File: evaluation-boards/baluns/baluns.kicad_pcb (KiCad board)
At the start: 4 copper layers, 23 x 100 mm, 178 parts, among them J1 CONN_COAXIAL, J10 CONN_COAXIAL, J11 CONN_COAXIAL, J12 CONN_COAXIAL, J13 CONN_COAXIAL, J14 CONN_COAXIAL, J15 CONN_COAXIAL, J16 CONN_COAXIAL, J17 CONN_COAXIAL, J18 CONN_COAXIAL, J2 CONN_COAXIAL, J3 CONN_COAXIAL, J4 CONN_COAXIAL, J5 CONN_COAXIAL, J6 CONN_COAXIAL, J7 CONN_COAXIAL, J8 CONN_COAXIAL, J9 CONN_COAXIAL, P1 Conn_01x02, P2 Conn_01x02, P3 Conn_01x02, P4 Conn_01x02, P5 Conn_01x02, Q1 BFR840, Q2 BFR840, Q3 BFR840, Q4 BFR840, Q5 BFP840ESD, Q6 BFP840ESD, Q7 BFP840ESD, Q8 BFP840ESD, T1 B0310J50100AHF, T2 B0310J50100AHF

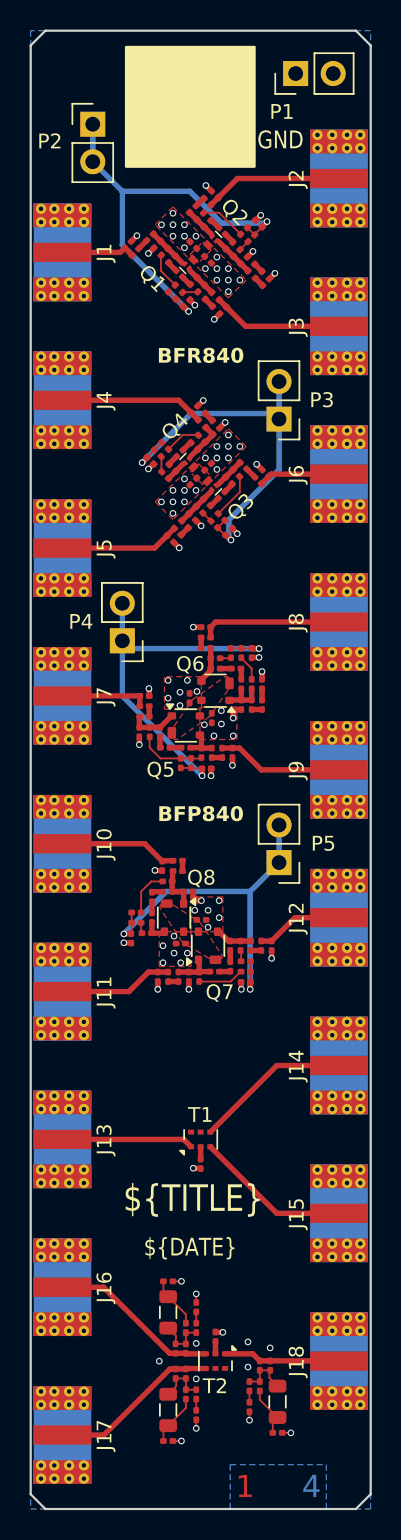
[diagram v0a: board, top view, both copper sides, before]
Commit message: Update baluns board
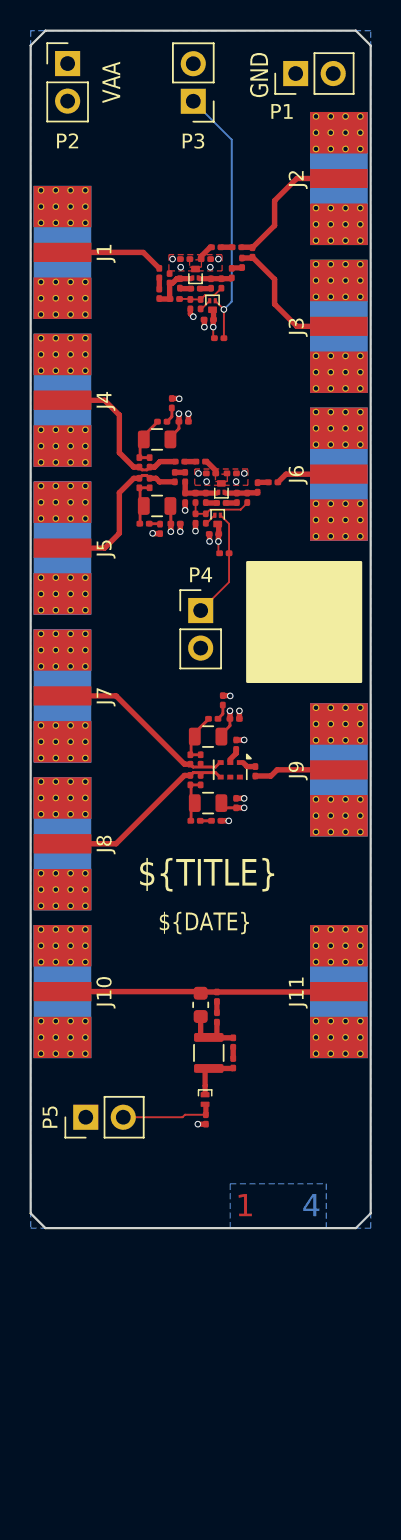
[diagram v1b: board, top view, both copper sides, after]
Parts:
- removed C10, C11, C12, C13, C17, C19, C20, C21, C22, C23, C24, C26, C27, C29, C31, C32, C35, C36, C37, C38, C39, C40, C44, C45, C47, C48, C7, C8, C9: 1 uF, Capacitor_SMD:C_0201_0603Metric
- removed C14, C15, C16, C18, C30, C33, C34, C43: 0.3 pF, Capacitor_SMD:C_0201_0603Metric
- removed J12, J13, J14, J15, J16, J17, J18: CONN_COAXIAL, sma-variants:SMA-EDGE-1.3mm-pad-1.05mm-gap-2.6mm-keepout
- removed L10: 18 nH, Inductor_SMD:L_0201_0603Metric
- removed L11: L, Inductor_SMD:L_0805_2012Metric
- removed L12, L9: L, Inductor_SMD:L_0201_0603Metric
- removed L14: 5.6 nH, Inductor_SMD:L_0201_0603Metric
- removed Q1, Q2, Q3, Q4: BFR840, eval:TSLP-3-9
- removed Q5, Q6, Q7, Q8: BFP840ESD, eval:SOT-343-4-3
- removed R10, R24, R46, R59, R71, R77, R79, R8, R80, R83: 220, Resistor_SMD:R_0201_0603Metric
- removed R11, R13, R19, R20, R26, R27, R30, R31, R32, R33, R36, R42, R47, R48, R49, R50, R51, R52, R55, R56, R60, R61, R62, R69, R72, R78, R81, R84, R85, R86: 0, Resistor_SMD:R_0201_0603Metric
- removed R14, R21, R37, R43, R6, R63, R73: 4.3k, Resistor_SMD:R_0201_0603Metric
- removed R15, R22, R38, R44, R64, R74, R9: 2.4k, Resistor_SMD:R_0201_0603Metric
- removed R16, R39, R66: 300, Resistor_SMD:R_0201_0603Metric
- removed R17, R40, R70: 200, Resistor_SMD:R_0201_0603Metric
- removed R18, R75, R82: 6.8k, Resistor_SMD:R_0201_0603Metric
- removed R23, R45, R7, R76: 470, Resistor_SMD:R_0201_0603Metric
- removed R25, R53: 43, Resistor_SMD:R_0201_0603Metric
- removed R28, R41, R54, R58, R67, R68: 82, Resistor_SMD:R_0201_0603Metric
- removed T1: B0310J50100AHF, RF_Converter:Anaren_0805_2012Metric-6
- added C112: 8p2, Capacitor_SMD:C_0201_0603Metric, F.Cu at (143.7, 133.4)
- added C171: 1 uF, Capacitor_SMD:C_0201_0603Metric, F.Cu at (141.8, 138.7)
- added C202: 2.2nF, Capacitor_SMD:C_0201_0603Metric, F.Cu at (138.9, 91.5)
- added C203: 8p2, Capacitor_SMD:C_0201_0603Metric, F.Cu at (137.7, 98.3)
- added C207: 1 uF, Capacitor_SMD:C_0201_0603Metric, F.Cu at (142.9, 97.0)
- added C208: 1 uF, Capacitor_SMD:C_0201_0603Metric, F.Cu at (144.3, 80.7)
- added C210: 1 uF, Capacitor_SMD:C_0201_0603Metric, F.Cu at (139.8, 95.2)
- added C211: 1 uF, Capacitor_SMD:C_0201_0603Metric, F.Cu at (141.2, 98.0)
- added C212: 1 uF, Capacitor_SMD:C_0201_0603Metric, F.Cu at (140.8, 83.5)
- added C213: 1 uF, Capacitor_SMD:C_0201_0603Metric, F.Cu at (143.9, 79.7)
- added C214: 1 uF, Capacitor_SMD:C_0201_0603Metric, F.Cu at (142.1, 84.5)
- added C215: 1 uF, Capacitor_SMD:C_0201_0603Metric, F.Cu at (142.4, 99.0)
- added D10: Schottky, eval:TSLP-2-19, F.Cu at (141.8, 137.3)
- added L19: 47uH, eval:L_Taiyo-Yuden_A251818, F.Cu at (142.1, 134.2)
- added L20: 33 nH, Inductor_SMD:L_0201_0603Metric, F.Cu at (142.6, 130.3)
- added L29: 100uH, eval:L_TDK_MLZ2012_h1.25mm, F.Cu at (138.6, 97.2)
- added L30: 56 nH, Inductor_SMD:L_0201_0603Metric, F.Cu at (138.1, 95.6)
- added Q15: BFR840, eval:TSLP-3-9, F.Cu at (141.2, 81.5)
- added Q16: Q_PMOS_GSD, eval:TSLP-3-9, F.Cu at (142.3, 83.5)
- added Q17: BFR840, eval:TSLP-3-9, F.Cu at (142.9, 96.0)
- added Q18: Q_PMOS_GSD, eval:TSLP-3-9, F.Cu at (142.7, 98.0)
- added R142: 0, Resistor_SMD:R_0201_0603Metric, F.Cu at (137.3, 95.6)
- added R143: 0, Resistor_SMD:R_0201_0603Metric, F.Cu at (138.8, 98.7)
- added R144: 0, Resistor_SMD:R_0201_0603Metric, F.Cu at (137.3, 94.2)
- added R147: 100, Resistor_SMD:R_0201_0603Metric, F.Cu at (139.6, 90.2)
- added R152: 330, Resistor_SMD:R_0201_0603Metric, F.Cu at (139.4, 81.8)
- added R153: 120, Resistor_SMD:R_0201_0603Metric, F.Cu at (140.1, 82.1)
- added R154: 33k, Resistor_SMD:R_0201_0603Metric, F.Cu at (142.8, 85.8)
- added R155: 100, Resistor_SMD:R_0201_0603Metric, F.Cu at (142.2, 82.1)
- added R156: 220, Resistor_SMD:R_0201_0603Metric, F.Cu at (142.9, 82.1)
- added R157: 750, Resistor_SMD:R_0201_0603Metric, F.Cu at (139.8, 83.2)
- added R158: 100, Resistor_SMD:R_0201_0603Metric, F.Cu at (141.8, 80.5)
- added R159: 100, Resistor_SMD:R_0201_0603Metric, F.Cu at (140.4, 80.5)
- added R160: 51, Resistor_SMD:R_0201_0603Metric, F.Cu at (143.6, 81.4)
- added R161: 10, Resistor_SMD:R_0201_0603Metric, F.Cu at (142.6, 79.7)
- added R162: 0, Resistor_SMD:R_0201_0603Metric, F.Cu at (138.7, 82.8)
- added R163: 0, Resistor_SMD:R_0201_0603Metric, F.Cu at (141.5, 83.5)
- added R164: 3.3k, Resistor_SMD:R_0201_0603Metric, F.Cu at (140.4, 96.6)
- added R165: 120, Resistor_SMD:R_0201_0603Metric, F.Cu at (141.8, 96.6)
- added R166: 100, Resistor_SMD:R_0201_0603Metric, F.Cu at (142.2, 95.0)
- added R167: 4k7, Resistor_SMD:R_0201_0603Metric, F.Cu at (141.2, 96.6)
- added R168: 100, Resistor_SMD:R_0201_0603Metric, F.Cu at (143.6, 95.0)
- added R169: 10, Resistor_SMD:R_0201_0603Metric, F.Cu at (141.5, 94.2)
- added R170: 10, Resistor_SMD:R_0201_0603Metric, F.Cu at (140.4, 95.2)
- added R171: 0, Resistor_SMD:R_0201_0603Metric, F.Cu at (141.8, 98.0)
- added R172: 0, Resistor_SMD:R_0201_0603Metric, F.Cu at (145.3, 95.9)
- added R173: 220, Resistor_SMD:R_0201_0603Metric, F.Cu at (144.7, 96.6)
- C1, C2, C5, C6: value 0.3 pF -> 1 uF
- C3: value 0.3 pF -> 8p2
- C4: value 0.3 pF -> 2.2nF
- J1, J10, J11, J2, J3, J4, J5, J6, J7, J8, J9: footprint sma-variants:SMA-EDGE-1.3mm-pad-1.05mm-gap-2.6mm-keepout -> eval:SMA_MyAntenna_A-SMA-KE-16.5A_EdgeMount
- L1: value 18 nH -> DNP
- L13: value L -> 62nH; footprint Inductor_SMD:L_0805_2012Metric -> Inductor_SMD:L_0603_1608Metric
- L2: value 5.6 nH -> 100uH; footprint Inductor_SMD:L_0201_0603Metric -> eval:L_TDK_MLZ2012_h1.25mm
- L3: value 18 nH -> 56 nH
- L4: value 5.6 nH -> 2.4 nH
- L5: value 18 nH -> 100uH; footprint Inductor_SMD:L_0201_0603Metric -> eval:L_TDK_MLZ2012_h1.25mm
- L6: value 5.6 nH -> 56 nH
- L7: value L -> 100uH; footprint Inductor_SMD:L_0201_0603Metric -> eval:L_TDK_MLZ2012_h1.25mm
- L8: value L -> 56 nH; footprint Inductor_SMD:L_0805_2012Metric -> Inductor_SMD:L_0201_0603Metric
- R1: value 82 -> 33k
- R12: value 0 -> 220
- R2: value 2.4k -> 0
- R3: value 4.3k -> 51
- R35: value 82 -> 220
- R4: value 300 -> 100
- R5: value 200 -> 10
- T2: value B0310J50100AHF -> RF_BALUN
- moved C49 62.7 mm to (140.1, 94.2), turned to 180 degrees
- moved R35 54.4 mm to (143.7, 134.8), turned to 90 degrees
- moved C42 50.2 mm to (140.3, 91.5), turned to 0 degrees
- moved L8 44.1 mm to (141.5, 114.3)
- moved L7 43.2 mm to (142.0, 112.8), turned to 180 degrees
- moved T2 40.0 mm to (143.5, 115.0)
- moved C3 39.2 mm to (141.2, 118.5), turned to 0 degrees
- moved R2 38.0 mm to (142.6, 118.5), turned to 180 degrees
- moved R5 36.7 mm to (140.8, 114.3), turned to -90 degrees
- moved R3 35.8 mm to (140.8, 115.7), turned to 90 degrees
- moved C2 35.5 mm to (143.8, 111.5), turned to 0 degrees
- moved C1 33.3 mm to (143.9, 117.2), turned to 90 degrees
- moved R4 31.7 mm to (143.0, 110.3), turned to 90 degrees
- moved C4 29.7 mm to (142.3, 111.5), turned to 180 degrees
- moved C41 29.1 mm to (139.8, 98.3), turned to 0 degrees
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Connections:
- C1 pad 1: Net-(J3-In) -> VAA
- C2 pad 1: Net-(J2-In) -> VAA
- C28 pad 1: Net-(J6-In) -> Net-(C28-Pad1)
- C28 pad 2: Net-(C28-Pad2) -> Net-(J1-In)
- C3 pad 1: Net-(J1-In) -> Net-(C3-Pad1)
- C3 pad 2: GND -> Net-(C3-Pad2)
- C4 pad 1: Net-(C21-Pad2) -> Net-(C4-Pad1)
- C4 pad 2: GND -> Net-(C4-Pad2)
- C41 pad 1: Net-(J12-In) -> VAA
- C41 pad 2: Net-(C41-Pad2) -> GND
- C42 pad 1: GND -> VAA
- C42 pad 2: Net-(T1-GND) -> GND
- C46 pad 2: Net-(Q1-B) -> Net-(J6-In)
- C49 pad 2: Net-(C49-Pad2) -> Net-(J4-In)
- C5 pad 1: Net-(J7-In) -> GND
- C5 pad 2: GND -> Net-(T2-GND)
- C6 pad 1: Net-(C6-Pad1) -> Net-(J9-In)
- C6 pad 2: GND -> Net-(C6-Pad2)
- J11 pad 1: Net-(J11-In) -> Net-(J10-In)
- L1 pad 1: Net-(C9-Pad1) -> Net-(J2-In)
- L1 pad 2: Net-(L1-Pad2) -> Net-(J3-In)
- L13 pad 1: Net-(C49-Pad1) -> Net-(C112-Pad2)
- L13 pad 2: Net-(L13-Pad2) -> Net-(J10-In)
- L2 pad 1: Net-(C11-Pad1) -> VAA
- L2 pad 2: Net-(L2-Pad2) -> Net-(C202-Pad2)
- L3 pad 1: Net-(L3-Pad1) -> Net-(C202-Pad2)
- L3 pad 2: Net-(Q4-C) -> Net-(J4-In)
- L5 pad 1: Net-(C37-Pad1) -> VAA
- L5 pad 2: Net-(L5-Pad2) -> Net-(C3-Pad1)
- L6 pad 1: Net-(C39-Pad1) -> Net-(C3-Pad1)
- L6 pad 2: Net-(L6-Pad2) -> Net-(J8-In)
- L7 pad 1: Net-(J17-In) -> VAA
- L7 pad 2: Net-(C47-Pad1) -> Net-(C4-Pad2)
- L8 pad 1: Net-(C47-Pad1) -> Net-(C4-Pad2)
- L8 pad 2: Net-(L8-Pad2) -> Net-(J7-In)
- P2 pad 1: Net-(P2-Pin_1) -> VAA
- P2 pad 2: Net-(P2-Pin_1) -> VAA
- P3 pad 2: Net-(P3-Pin_1) -> GND
- P4 pad 2: Net-(P4-Pin_1) -> GND
- P5 pad 1: Net-(P5-Pin_1) -> VAA
- P5 pad 2: Net-(P5-Pin_1) -> Net-(D10-A)
- R1 pad 1: GND -> VAA
- R1 pad 2: Net-(Q1-E) -> Net-(P4-Pin_1)
- R12 pad 2: Net-(Q6-B) -> Net-(C112-Pad2)
- R2 pad 2: Net-(Q2-B) -> Net-(C3-Pad2)
- R3 pad 1: Net-(Q2-B) -> Net-(C3-Pad1)
- R3 pad 2: Net-(R19-Pad2) -> Net-(J8-In)
- R35 pad 1: GND -> Net-(D10-K)
- R35 pad 2: Net-(Q1-E) -> Net-(C112-Pad1)
- R4 pad 1: Net-(C45-Pad1) -> Net-(C4-Pad1)
- R4 pad 2: Net-(L10-Pad1) -> GND
- R5 pad 1: Net-(Q2-C) -> Net-(C4-Pad2)
- R5 pad 2: Net-(R47-Pad2) -> Net-(J7-In)
- T2 pad 1: Net-(J18-In) -> Net-(C6-Pad2)
- T2 pad 3: Net-(J16-In) -> Net-(J7-In)
- T2 pad 4: Net-(J17-In) -> Net-(J8-In)
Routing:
- net Net-(P2-Pin_1): track 29.9 -> 0.00 mm, vias 2 -> 0
- net Net-(P5-Pin_1): track 25.5 -> 0.00 mm, vias 2 -> 0
- net Net-(P4-Pin_1): track 27.2 -> 7.49 mm, vias 2 -> 0
- net GND: track 21.1 -> 7.98 mm, vias 98 -> 23
- net Net-(J17-In): track 11.6 -> 0.00 mm
- net Net-(J16-In): track 11.6 -> 0.00 mm
- net VAA: track 0.00 -> 11.5 mm, vias 0 -> 6
- net Net-(J10-In): track 7.98 -> 18.8 mm
- net Net-(J15-In): track 10.6 -> 0.00 mm
- net Net-(J14-In): track 10.6 -> 0.00 mm
- net Net-(J13-In): track 8.91 -> 0.00 mm
- net Net-(P3-Pin_1): track 26.8 -> 18.1 mm, vias 2 -> 1
- net Net-(J18-In): track 7.91 -> 0.00 mm
- net Net-(J11-In): track 7.70 -> 0.00 mm
- net Net-(J7-In): track 5.93 -> 12.8 mm
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- added copper zone on F.Cu, net Net-(Q15-E)
- added copper zone on F.Cu, net Net-(Q17-E)
- added copper zone on In2.Cu, net VAA
- removed copper zone on In2.Cu, net GND
- removed copper zone on F.Cu, net Net-(Q1-E)
- removed copper zone on F.Cu, net Net-(Q3-E)
- removed copper zone on F.Cu, net Net-(Q5-E)
- removed copper zone on F.Cu, net Net-(Q7-E)
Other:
- board size 23 x 100 mm -> 23 x 81 mm
- board text added: "VAA"
- board text removed: "BFP840"
- board text removed: "BFR840"
- board text removed: "R1"
- board text removed: "R35"
